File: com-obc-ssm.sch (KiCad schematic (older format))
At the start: 0 parts

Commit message: obc updated
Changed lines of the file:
@@
 $EndSheet
 $Sheet
-S 6350 2450 1900 1150
-U 5A07580F
+S 6050 3000 1950 650
+U 5A076FE1
 F0 "obc" 60
 F1 "obc-ssm.sch" 60

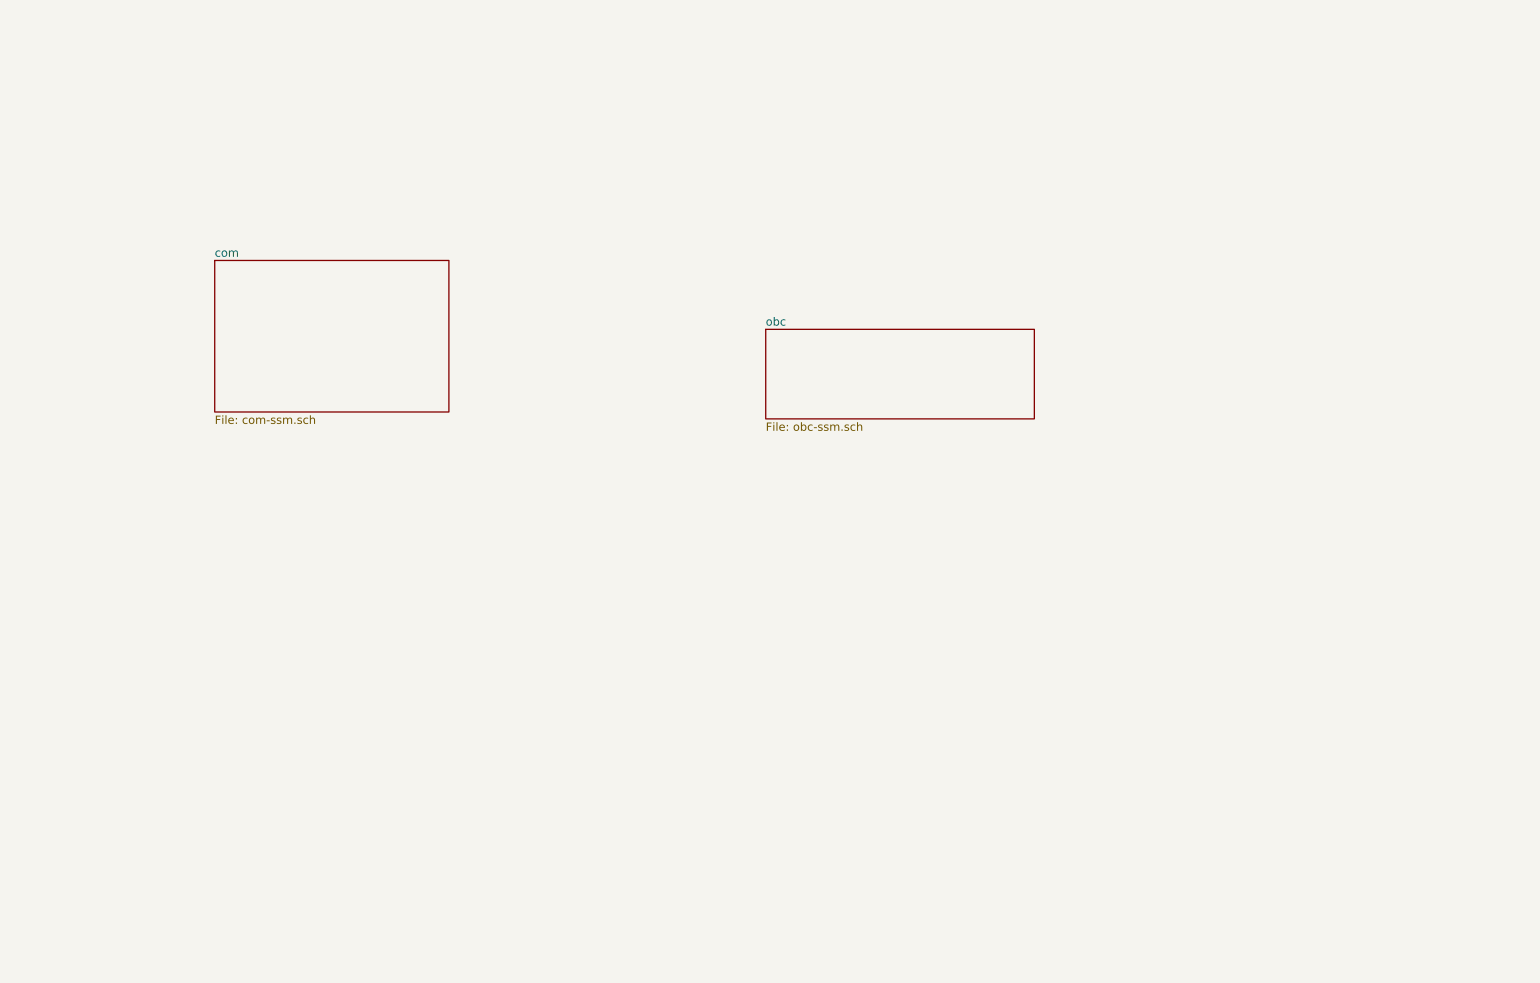
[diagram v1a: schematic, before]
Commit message: combined schematic into one board - prelim
still need to connect to other boards
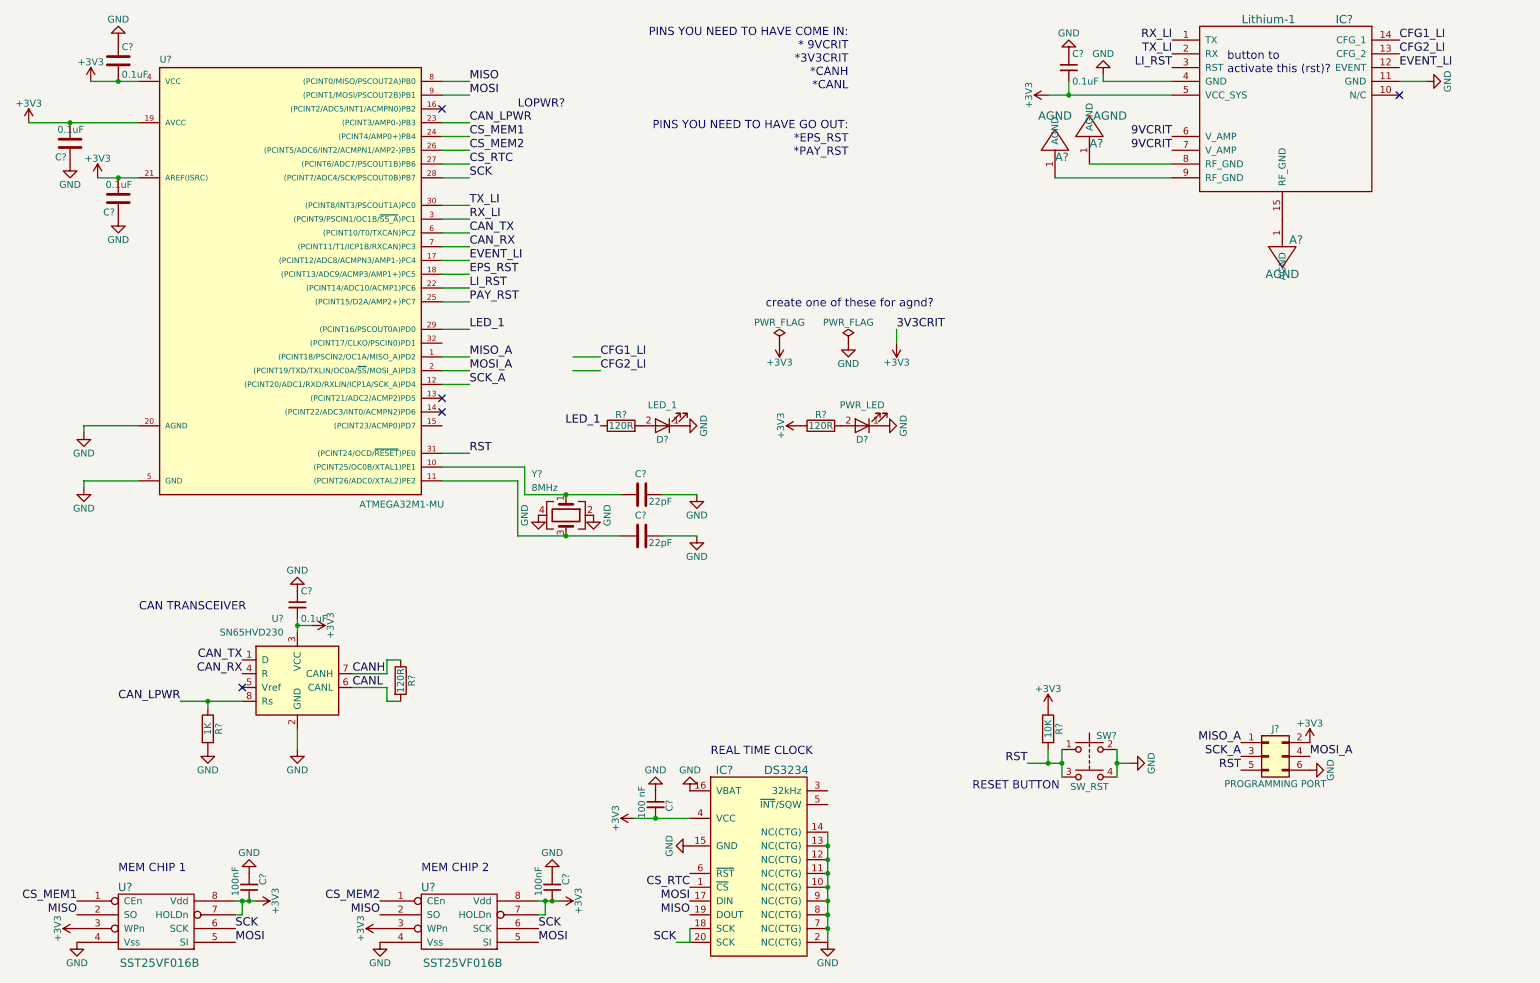
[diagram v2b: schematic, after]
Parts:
- added A? (x3): AGND, symbol AGND
- added C? (x2): 100nF, Capacitors_SMD:C_0603, symbol C_Small
- added C? (x2): 0.1uF, symbol C_Small
- added C? (x2): 22pF, symbol C
- added C? (x3): 0.1uF, symbol C
- added C?: 100 nF, symbol C_Small
- added D?: PWR_LED, symbol LED
- added D?: LED_1, symbol LED
- added IC?: DS3234, Housings_SOIC:SOIC-20W_7.5x12.8mm_Pitch1.27mm, symbol DS3234
- added IC?: Lithium-1, symbol Lithium-1
- added J?: PROGRAMMING PORT, symbol Conn_02x03_Odd_Even
- added R? (x3): 120R, symbol R
- added R?: 1K, symbol R
- added R?: 10K, symbol R
- added SW?: SW_RST, symbol SW_Push_Dual
- added U? (x2): SST25VF016B, Housings_SOIC:SOIC-8_3.9x4.9mm_Pitch1.27mm, symbol SST25VF016B
- added U?: SN65HVD230, Housings_SOIC:SOIC-8_3.9x4.9mm_Pitch1.27mm, symbol SN65HVD230
- added U?: ATMEGA32M1-MU, QFN32, symbol ATMEGA32M1-MU
- added Y?: 8MHz, symbol Crystal_GND24
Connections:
- new net: C?.2, U?.10 ((PCINT25/OC0B/XTAL1)PE1), Y?.1
- new net: C?.2, U?.11 ((PCINT26/ADC0/XTAL2)PE2), Y?.3
- new net: D?.2 (A), R?.2 (x2)
- new net: A?.1 (AGND), IC?.15 (RF_GND)
- new net: A?.1 (AGND), IC?.8 (RF_GND)
- new net: A?.1 (AGND), IC?.9 (RF_GND)
- new net +3V3: C?.1, C?.1, C?.2, C?.2, C?.2, C?.2, C?.2, C?.2, IC?.4 (VCC), IC?.5 (VCC_SYS), J?.2 (Pin_2), R?.1, R?.1, U?.19 (AVCC), U?.21 (AREF(ISRC)), U?.3 (VCC), U?.3 (WPn), U?.3 (WPn), U?.4 (VCC), U?.7 (HOLDn), U?.7 (HOLDn), U?.8 (Vdd), U?.8 (Vdd)
- new net 9VCRIT: IC?.6 (V_AMP), IC?.7 (V_AMP)
- new net CANH: R?.1, U?.7 (CANH)
- new net CANL: R?.2, U?.6 (CANL)
- new net CAN_LPWR: R?.1, U?.23 ((PCINT3/AMP0-)PB3), U?.8 (Rs)
- new net CAN_RX: U?.4 (R), U?.7 ((PCINT11/T1/ICP1B/RXCAN)PC3)
- new net CAN_TX: U?.1 (D), U?.6 ((PCINT10/T0/TXCAN)PC2)
- new net CFG1_LI: IC?.14 (CFG_1)
- new net CFG2_LI: IC?.13 (CFG_2)
- new net CS_MEM1: U?.1 (CEn), U?.24 ((PCINT4/AMP0+)PB4)
- new net CS_MEM2: U?.1 (CEn), U?.26 ((PCINT5/ADC6/INT2/ACMPN1/AMP2-)PB5)
- new net CS_RTC: IC?.1 (~CS~), U?.27 ((PCINT6/ADC7/PSCOUT1B)PB6)
- new net EPS_RST: U?.18 ((PCINT13/ADC9/ACMP3/AMP1+)PC5)
- new net EVENT_LI: IC?.12 (EVENT), U?.17 ((PCINT12/ADC8/ACMPN3/AMP1-)PC4)
- new net GND: C?.1, C?.1, C?.1, C?.1, C?.1, C?.1, C?.1, C?.1, C?.2, C?.2, D?.1 (K), D?.1 (K), IC?.10 (NC(CTG)), IC?.11 (GND), IC?.11 (NC(CTG)), IC?.12 (NC(CTG)), IC?.13 (NC(CTG)), IC?.14 (NC(CTG)), IC?.15 (GND), IC?.16 (VBAT), IC?.2 (NC(CTG)), IC?.4 (GND), IC?.7 (NC(CTG)), IC?.8 (NC(CTG)), IC?.9 (NC(CTG)), J?.6 (Pin_6), R?.2, SW?.2, SW?.4, U?.2 (GND), U?.20 (AGND), U?.4 (Vss), U?.4 (Vss), U?.5 (GND), Y?.2, Y?.4
- new net LED_1: R?.1, U?.29 ((PCINT16/PSCOUT0A)PD0)
- new net LI_RST: IC?.3 (RST), U?.22 ((PCINT14/ADC10/ACMP1)PC6)
- new net MISO: IC?.19 (DOUT), U?.2 (SO), U?.2 (SO), U?.8 ((PCINT0/MISO/PSCOUT2A)PB0)
- new net MISO_A: J?.1 (Pin_1), U?.1 ((PCINT18/PSCIN2/OC1A/MISO_A)PD2)
- new net MOSI: IC?.17 (DIN), U?.5 (SI), U?.5 (SI), U?.9 ((PCINT1/MOSI/PSCOUT2B)PB1)
- new net MOSI_A: J?.4 (Pin_4), U?.2 ((PCINT19/TXD/TXLIN/OC0A/~SS~/MOSI_A)PD3)
- new net PAY_RST: U?.25 ((PCINT15/D2A/AMP2+)PC7)
- new net RST: J?.5 (Pin_5), R?.2, SW?.1, SW?.3, U?.31 ((PCINT24/OCD/~RESET~)PE0)
- new net RX_LI: IC?.1 (TX), U?.3 ((PCINT9/PSCIN1/OC1B/~SS_A~)PC1)
- new net SCK: IC?.18 (SCK), IC?.20 (SCK), U?.28 ((PCINT7/ADC4/SCK/PSCOUT0B)PB7), U?.6 (SCK), U?.6 (SCK)
- new net SCK_A: J?.3 (Pin_3), U?.12 ((PCINT20/ADC1/RXD/RXLIN/ICP1A/SCK_A)PD4)
- new net TX_LI: IC?.2 (RX), U?.30 ((PCINT8/INT3/PSCOUT1A)PC0)
- no-connect marks 0 -> 5
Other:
- note added: "CAN TRANSCEIVER"
- note added: "LOPWR?"
- note added: "MEM CHIP 1"
- note added: "MEM CHIP 2"
- note added: "PINS YOU NEED TO HAVE COME IN:\n* 9VCRIT\n*3V3CRIT\n*CANH\n*CANL\n\n\nPINS YOU NEED TO HAVE GO OUT:\n*EPS_RST\n*PAY_RST"
- note added: "REAL TIME CLOCK"
- note added: "RESET BUTTON"
- note added: "button to\nactivate this (rst)?"
- note added: "create one of these for agnd?"

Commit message: li-1 changes
* Still need to figure out how we're interfacing with/configuring Li-1
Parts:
- added R?: 10K, symbol R
- added SW?: SW_RST, symbol SW_Push_Dual
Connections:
- wire segments 71 -> 76
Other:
- note added: "LI-1 RESET BUTTON"
- note added: "NEED A HEADER TO CONFIGURE LI-1"
- note added: "OBC RESET BUTTON"
- note added: "need to figure out how we're interfacing with li-1"
- note removed: "RESET BUTTON"
- note removed: "button to\nactivate this (rst)?"
- moved on the sheet: J?, R?, SW?
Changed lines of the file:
@@
 Text Label 3900 2400 0    60   ~ 0
 CAN_RX
-Text Label 4850 3200 0    60   ~ 0
+Text Label 9750 4900 0    60   ~ 0
 CFG1_LI
-Text Label 4850 3300 0    60   ~ 0
+Text Label 9750 5000 0    60   ~ 0
 CFG2_LI
 $Comp
@@
 	1    0    0    -1
 $EndComp
-Text Label 3900 2500 0    60   ~ 0
+Text Label 9700 5150 0    60   ~ 0
 EVENT_LI
 Text Label 3900 3000 0    60   ~ 0
@@
 L SW_Push_Dual SW?
 U 1 1 5A077CDE
-P 8400 6050
-F 0 "SW?" H 8450 6150 50  0000 L CNN
-F 1 "SW_RST" H 8400 5780 50  0000 C CNN
-F 2 "" H 8400 6250 50  0001 C CNN
-F 3 "" H 8400 6250 50  0001 C CNN
-	1    8400 6050
-	1    0    0    -1
-$EndComp
-Wire Wire Line
-	8200 6050 8200 6250
-Wire Wire Line
-	7950 6150 8200 6150
-Connection ~ 8200 6150
-Connection ~ 8100 6150
-Wire Wire Line
-	8100 6050 8100 6150
-Text Label 7950 6150 2    60   ~ 0
+P 7800 6150
+F 0 "SW?" H 7850 6250 50  0000 L CNN
+F 1 "SW_RST" H 7800 5880 50  0000 C CNN
+F 2 "" H 7800 6350 50  0001 C CNN
+F 3 "" H 7800 6350 50  0001 C CNN
+	1    7800 6150
+	1    0    0    -1
+$EndComp
+Wire Wire Line
+	7600 6150 7600 6350
+Wire Wire Line
+	7350 6250 7600 6250
+Connection ~ 7600 6250
+Connection ~ 7500 6250
+Wire Wire Line
+	7500 6150 7500 6250
+Text Label 7350 6250 2    60   ~ 0
 RST
 $Comp
 L R R?
 U 1 1 5A092CCA
-P 8100 5900
-F 0 "R?" V 8180 5900 50  0000 C CNN
-F 1 "10K" V 8100 5900 50  0000 C CNN
-F 2 "" V 8030 5900 50  0001 C CNN
-F 3 "" H 8100 5900 50  0001 C CNN
-	1    8100 5900
+P 7500 6000
+F 0 "R?" V 7580 6000 50  0000 C CNN
+F 1 "10K" V 7500 6000 50  0000 C CNN
+F 2 "" V 7430 6000 50  0001 C CNN
+F 3 "" H 7500 6000 50  0001 C CNN
+	1    7500 6000
 	1    0    0    -1
 $EndComp
@@
 L +3V3 #PWR?
 U 1 1 5A092D38
-P 8100 5750
-F 0 "#PWR?" H 8100 5600 50  0001 C CNN
-F 1 "+3V3" H 8100 5890 50  0000 C CNN
-F 2 "" H 8100 5750 50  0001 C CNN
-F 3 "" H 8100 5750 50  0001 C CNN
-	1    8100 5750
-	1    0    0    -1
-$EndComp
-Wire Wire Line
-	8600 6250 8600 6050
-Wire Wire Line
-	8600 6150 8700 6150
-Connection ~ 8600 6150
+P 7500 5850
+F 0 "#PWR?" H 7500 5700 50  0001 C CNN
+F 1 "+3V3" H 7500 5990 50  0000 C CNN
+F 2 "" H 7500 5850 50  0001 C CNN
+F 3 "" H 7500 5850 50  0001 C CNN
+	1    7500 5850
+	1    0    0    -1
+$EndComp
+Wire Wire Line
+	8000 6350 8000 6150
+Wire Wire Line
+	8000 6250 8100 6250
+Connection ~ 8000 6250
 $Comp
 L GND #PWR?
 U 1 1 5A092E0A
-P 8700 6150
-F 0 "#PWR?" H 8700 5900 50  0001 C CNN
-F 1 "GND" H 8700 6000 50  0000 C CNN
-F 2 "" H 8700 6150 50  0001 C CNN
-F 3 "" H 8700 6150 50  0001 C CNN
-	1    8700 6150
+P 8100 6250
+F 0 "#PWR?" H 8100 6000 50  0001 C CNN
+F 1 "GND" H 8100 6100 50  0000 C CNN
+F 2 "" H 8100 6250 50  0001 C CNN
+F 3 "" H 8100 6250 50  0001 C CNN
+	1    8100 6250
 	0    -1   -1   0
 $EndComp
@@
 L Conn_02x03_Odd_Even J?
 U 1 1 5A092E36
-P 9700 6100
-F 0 "J?" H 9750 6300 50  0000 C CNN
-F 1 "PROGRAMMING PORT" H 9750 5900 50  0000 C CNN
-F 2 "" H 9700 6100 50  0001 C CNN
-F 3 "" H 9700 6100 50  0001 C CNN
-	1    9700 6100
-	1    0    0    -1
-$EndComp
-Text Label 9500 6000 2    60   ~ 0
+P 10400 6100
+F 0 "J?" H 10450 6300 50  0000 C CNN
+F 1 "PROGRAMMING PORT" H 10450 5900 50  0000 C CNN
+F 2 "" H 10400 6100 50  0001 C CNN
+F 3 "" H 10400 6100 50  0001 C CNN
+	1    10400 6100
+	1    0    0    -1
+$EndComp
+Text Label 10200 6000 2    60   ~ 0
 MISO_A
-Text Label 9500 6100 2    60   ~ 0
+Text Label 10200 6100 2    60   ~ 0
 SCK_A
-Text Label 9500 6200 2    60   ~ 0
+Text Label 10200 6200 2    60   ~ 0
 RST
-Text Label 10000 6100 0    60   ~ 0
+Text Label 10700 6100 0    60   ~ 0
 MOSI_A
 $Comp
 L +3V3 #PWR?
 U 1 1 5A093004
-P 10000 6000
-F 0 "#PWR?" H 10000 5850 50  0001 C CNN
-F 1 "+3V3" H 10000 6140 50  0000 C CNN
-F 2 "" H 10000 6000 50  0001 C CNN
-F 3 "" H 10000 6000 50  0001 C CNN
-	1    10000 6000
+P 10700 6000
+F 0 "#PWR?" H 10700 5850 50  0001 C CNN
+F 1 "+3V3" H 10700 6140 50  0000 C CNN
+F 2 "" H 10700 6000 50  0001 C CNN
+F 3 "" H 10700 6000 50  0001 C CNN
+	1    10700 6000
 	1    0    0    -1
 $EndComp
@@
 L GND #PWR?
 U 1 1 5A093032
-P 10000 6200
-F 0 "#PWR?" H 10000 5950 50  0001 C CNN
-F 1 "GND" H 10000 6050 50  0000 C CNN
-F 2 "" H 10000 6200 50  0001 C CNN
-F 3 "" H 10000 6200 50  0001 C CNN
-	1    10000 6200
+P 10700 6200
+F 0 "#PWR?" H 10700 5950 50  0001 C CNN
+F 1 "GND" H 10700 6050 50  0000 C CNN
+F 2 "" H 10700 6200 50  0001 C CNN
+F 3 "" H 10700 6200 50  0001 C CNN
+	1    10700 6200
 	0    -1   -1   0
 $EndComp
@@
 	1    0    0    -1
 $EndComp
-Text Notes 7550 6350 0    60   ~ 0
-RESET BUTTON
+Text Notes 7200 5600 0    60   ~ 0
+OBC RESET BUTTON
 $Comp
 L AGND A?
@@
 	3900 2400 3700 2400
 Wire Wire Line
-	3700 2500 3900 2500
-Wire Wire Line
-	4650 3200 4850 3200
-Wire Wire Line
-	4850 3300 4650 3300
+	9500 5150 9700 5150
+Wire Wire Line
+	9550 4900 9750 4900
+Wire Wire Line
+	9750 5000 9550 5000
 Wire Wire Line
 	3700 3200 3900 3200
@@
 Wire Wire Line
 	3900 2800 3700 2800
-Text Notes 9400 1150 0    60   ~ 0
-button to\nactivate this (rst)?
 Wire Wire Line
 	2650 5100 2650 5200
@@
 Wire Wire Line
 	2650 5900 2650 6050
+Text Notes 9150 4700 0    60   ~ 0
+NEED A HEADER TO CONFIGURE LI-1
+$Comp
+L SW_Push_Dual SW?
+U 1 1 5A10C86E
+P 9250 6150
+F 0 "SW?" H 9300 6250 50  0000 L CNN
+F 1 "SW_RST" H 9250 5880 50  0000 C CNN
+F 2 "" H 9250 6350 50  0001 C CNN
+F 3 "" H 9250 6350 50  0001 C CNN
+	1    9250 6150
+	1    0    0    -1
+$EndComp
+Wire Wire Line
+	9050 6150 9050 6350
+Wire Wire Line
+	8800 6250 9050 6250
+Connection ~ 9050 6250
+Connection ~ 8950 6250
+Wire Wire Line
+	8950 6150 8950 6250
+Text Label 8800 6250 2    60   ~ 0
+RST
+$Comp
+L R R?
+U 1 1 5A10C87A
+P 8950 6000
+F 0 "R?" V 9030 6000 50  0000 C CNN
+F 1 "10K" V 8950 6000 50  0000 C CNN
+F 2 "" V 8880 6000 50  0001 C CNN
+F 3 "" H 8950 6000 50  0001 C CNN
+	1    8950 6000
+	1    0    0    -1
+$EndComp
+$Comp
+L +3V3 #PWR?
+U 1 1 5A10C880
+P 8950 5850
+F 0 "#PWR?" H 8950 5700 50  0001 C CNN
+F 1 "+3V3" H 8950 5990 50  0000 C CNN
+F 2 "" H 8950 5850 50  0001 C CNN
+F 3 "" H 8950 5850 50  0001 C CNN
+	1    8950 5850
+	1    0    0    -1
+$EndComp
+Wire Wire Line
+	9450 6350 9450 6150
+Wire Wire Line
+	9450 6250 9550 6250
+Connection ~ 9450 6250
+$Comp
+L GND #PWR?
+U 1 1 5A10C889
+P 9550 6250
+F 0 "#PWR?" H 9550 6000 50  0001 C CNN
+F 1 "GND" H 9550 6100 50  0000 C CNN
+F 2 "" H 9550 6250 50  0001 C CNN
+F 3 "" H 9550 6250 50  0001 C CNN
+	1    9550 6250
+	0    -1   -1   0
+$EndComp
+Text Notes 8600 5600 0    60   ~ 0
+LI-1 RESET BUTTON
+Text Notes 8700 4600 0    60   ~ 0
+need to figure out how we're interfacing with li-1
 $EndSCHEMATC
